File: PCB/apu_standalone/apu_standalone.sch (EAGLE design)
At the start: 95 parts, among them IC1 74AHC573, IC10 DAC, IC11 IS62C1024AL, IC12 ATMEGA2560, IC15 FT232RL, IC2 4050D, IC3 DS1307, IC4 LP298XS, IC5 S-SMP, IC6 S-DSP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

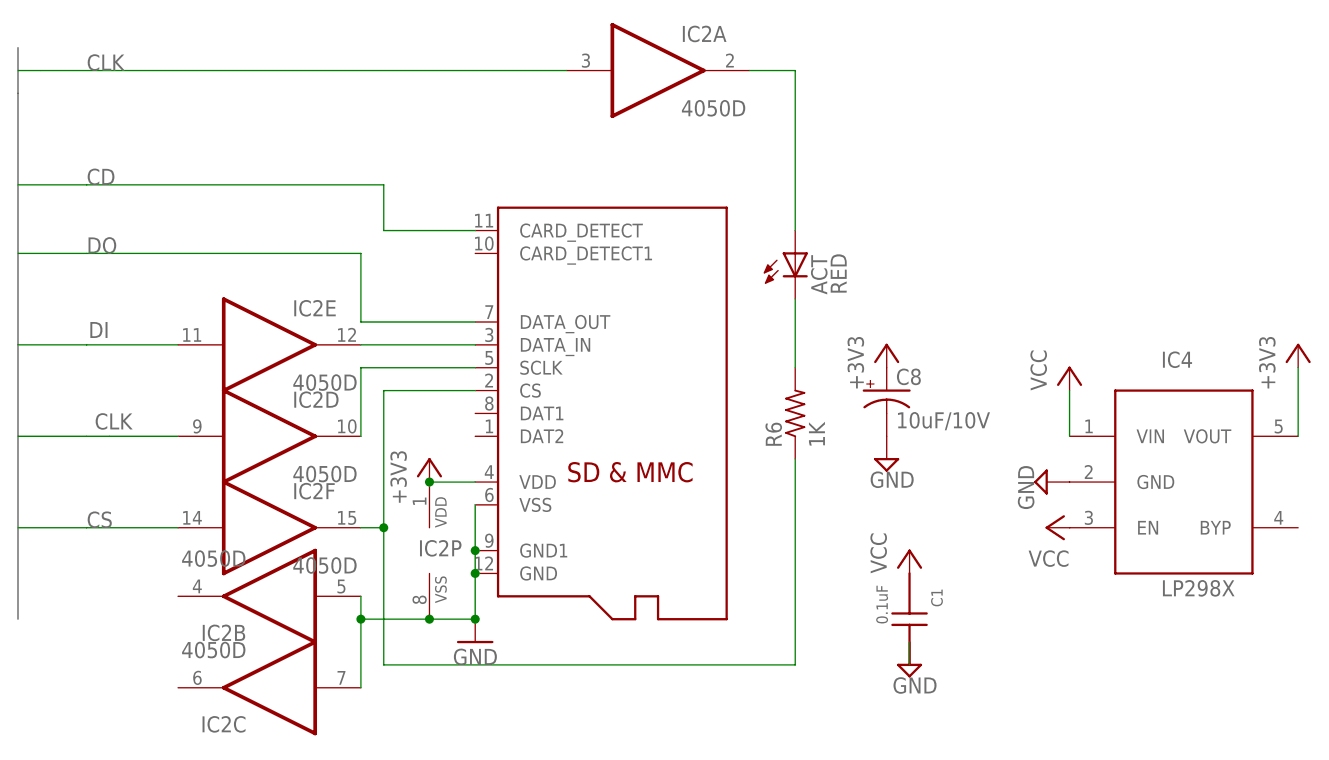
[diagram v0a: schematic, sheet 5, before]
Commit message: PC Side communications
Added various commands for a planned total rewrite of the PC side
client,.
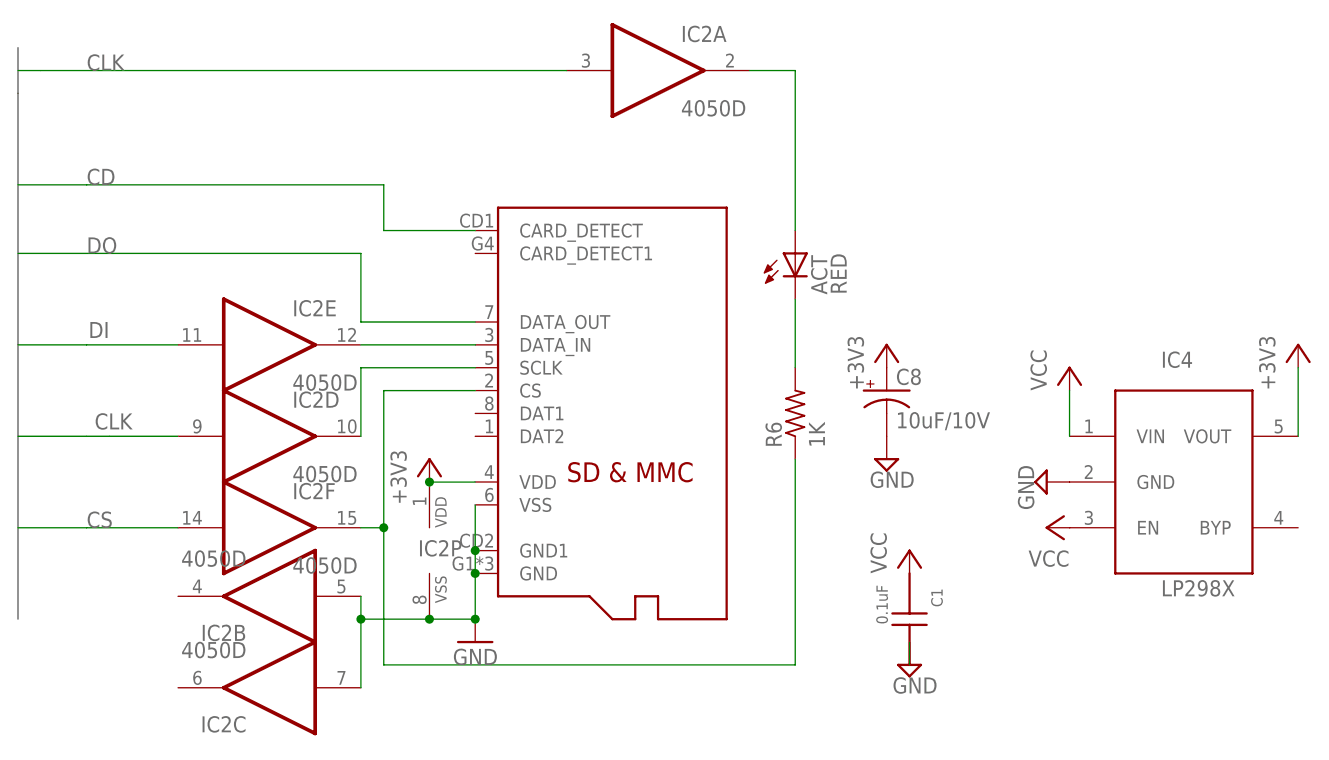
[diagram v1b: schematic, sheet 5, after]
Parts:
- X1: value MICROSDMOLEX -> MICROSDMOLEX-2; device adafruit:MICROSDMOLEX -> adafruit:MICROSDMOLEX-2
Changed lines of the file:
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@@
 <grid distance="0.1" unitdist="inch" unit="inch" style="lines" multiple="1" display="no" altdistance="0.01" altunitdist="inch" altunit="inch"/>
 <layers>
-<layer number="1" name="Top" color="4" fill="1" visible="no" active="no"/>
-<layer number="2" name="Route2" color="1" fill="3" visible="no" active="no"/>
-<layer number="3" name="Route3" color="4" fill="3" visible="no" active="no"/>
-<layer number="4" name="Route4" color="1" fill="4" visible="no" active="no"/>
-<layer number="5" name="Route5" color="4" fill="4" visible="no" active="no"/>
-<layer number="6" name="Route6" color="1" fill="8" visible="no" active="no"/>
-<layer number="7" name="Route7" color="4" fill="8" visible="no" active="no"/>
-<layer number="8" name="Route8" color="1" fill="2" visible="no" active="no"/>
-<layer number="9" name="Route9" color="4" fill="2" visible="no" active="no"/>
-<layer number="10" name="Route10" color="1" fill="7" visible="no" active="no"/>
-<layer number="11" name="Route11" color="4" fill="7" visible="no" active="no"/>
-<layer number="12" name="Route12" color="1" fill="5" visible="no" active="no"/>
-<layer number="13" name="Route13" color="4" fill="5" visible="no" active="no"/>
-<layer number="14" name="Route14" color="1" fill="6" visible="no" active="no"/>
-<layer number="15" name="Route15" color="4" fill="6" visible="no" active="no"/>
-<layer number="16" name="Bottom" color="1" fill="1" visible="no" active="no"/>
-<layer number="17" name="Pads" color="2" fill="1" visible="no" active="no"/>
-<layer number="18" name="Vias" color="2" fill="1" visible="no" active="no"/>
-<layer number="19" name="Unrouted" color="6" fill="1" visible="no" active="no"/>
-<layer number="20" name="Dimension" color="15" fill="1" visible="no" active="no"/>
-<layer number="21" name="tPlace" color="7" fill="1" visible="no" active="no"/>
-<layer number="22" name="bPlace" color="7" fill="1" visible="no" active="no"/>
-<layer number="23" name="tOrigins" color="15" fill="1" visible="no" active="no"/>
-<layer number="24" name="bOrigins" color="15" fill="1" visible="no" active="no"/>
-<layer number="25" name="tNames" color="7" fill="1" visible="no" active="no"/>
-<layer number="26" name="bNames" color="7" fill="1" visible="no" active="no"/>
-<layer number="27" name="tValues" color="7" fill="1" visible="no" active="no"/>
-<layer number="28" name="bValues" color="7" fill="1" visible="no" active="no"/>
+<layer number="1" name="Top" color="4" fill="1" visible="yes" active="no"/>
+<layer number="2" name="Route2" color="1" fill="3" visible="yes" active="no"/>
+<layer number="3" name="Route3" color="4" fill="3" visible="yes" active="no"/>
+<layer number="4" name="Route4" color="1" fill="4" visible="yes" active="no"/>
+<layer number="5" name="Route5" color="4" fill="4" visible="yes" active="no"/>
+<layer number="6" name="Route6" color="1" fill="8" visible="yes" active="no"/>
+<layer number="7" name="Route7" color="4" fill="8" visible="yes" active="no"/>
+<layer number="8" name="Route8" color="1" fill="2" visible="yes" active="no"/>
+<layer number="9" name="Route9" color="4" fill="2" visible="yes" active="no"/>
+<layer number="10" name="Route10" color="1" fill="7" visible="yes" active="no"/>
+<layer number="11" name="Route11" color="4" fill="7" visible="yes" active="no"/>
+<layer number="12" name="Route12" color="1" fill="5" visible="yes" active="no"/>
+<layer number="13" name="Route13" color="4" fill="5" visible="yes" active="no"/>
+<layer number="14" name="Route14" color="1" fill="6" visible="yes" active="no"/>
+<layer number="15" name="Route15" color="4" fill="6" visible="yes" active="no"/>
+<layer number="16" name="Bottom" color="1" fill="1" visible="yes" active="no"/>
+<layer number="17" name="Pads" color="2" fill="1" visible="yes" active="no"/>
+<layer number="18" name="Vias" color="22" fill="1" visible="yes" active="no"/>
+<layer number="19" name="Unrouted" color="6" fill="1" visible="yes" active="no"/>
+<layer number="20" name="Dimension" color="15" fill="1" visible="yes" active="no"/>
+<layer number="21" name="tPlace" color="7" fill="1" visible="yes" active="no"/>
+<layer number="22" name="bPlace" color="7" fill="1" visible="yes" active="no"/>
+<layer number="23" name="tOrigins" color="15" fill="1" visible="yes" active="no"/>
+<layer number="24" name="bOrigins" color="15" fill="1" visible="yes" active="no"/>
+<layer number="25" name="tNames" color="7" fill="1" visible="yes" active="no"/>
+<layer number="26" name="bNames" color="7" fill="1" visible="yes" active="no"/>
+<layer number="27" name="tValues" color="7" fill="1" visible="yes" active="no"/>
+<layer number="28" name="bValues" color="7" fill="1" visible="yes" active="no"/>
 <layer number="29" name="tStop" color="7" fill="3" visible="no" active="no"/>
 <layer number="30" name="bStop" color="7" fill="6" visible="no" active="no"/>
@@
 <layer number="35" name="tGlue" color="7" fill="4" visible="no" active="no"/>
 <layer number="36" name="bGlue" color="7" fill="5" visible="no" active="no"/>
-<layer number="37" name="tTest" color="7" fill="1" visible="no" active="no"/>
-<layer number="38" name="bTest" color="7" fill="1" visible="no" active="no"/>
+<layer number="37" name="tTest" color="7" fill="1" visible="yes" active="no"/>
+<layer number="38" name="bTest" color="7" fill="1" visible="yes" active="no"/>
 <layer number="39" name="tKeepout" color="4" fill="11" visible="no" active="no"/>
 <layer number="40" name="bKeepout" color="1" fill="11" visible="no" active="no"/>
@@
 <layer number="44" name="Drills" color="7" fill="1" visible="no" active="no"/>
 <layer number="45" name="Holes" color="7" fill="1" visible="no" active="no"/>
-<layer number="46" name="Milling" color="3" fill="1" visible="no" active="no"/>
-<layer number="47" name="Measures" color="7" fill="1" visible="no" active="no"/>
-<layer number="48" name="Document" color="7" fill="1" visible="no" active="no"/>
-<layer number="49" name="Reference" color="7" fill="1" visible="no" active="no"/>
-<layer number="50" name="dxf" color="7" fill="1" visible="no" active="no"/>
-<layer number="51" name="tDocu" color="7" fill="1" visible="no" active="no"/>
-<layer number="52" name="bDocu" color="7" fill="1" visible="no" active="no"/>
-<layer number="53" name="tGND_GNDA" color="7" fill="9" visible="no" active="no"/>
-<layer number="54" name="bGND_GNDA" color="1" fill="9" visible="no" active="no"/>
-<layer number="56" name="wert" color="7" fill="1" visible="no" active="no"/>
+<layer number="46" name="Milling" color="3" fill="1" visible="yes" active="no"/>
+<layer number="47" name="Measures" color="7" fill="1" visible="yes" active="no"/>
+<layer number="48" name="Document" color="7" fill="1" visible="yes" active="no"/>
+<layer number="49" name="Reference" color="7" fill="1" visible="yes" active="no"/>
+<layer number="50" name="dxf" color="7" fill="1" visible="yes" active="no"/>
+<layer number="51" name="tDocu" color="7" fill="1" visible="yes" active="no"/>
+<layer number="52" name="bDocu" color="7" fill="1" visible="yes" active="no"/>
+<layer number="53" name="tGND_GNDA" color="7" fill="9" visible="yes" active="no"/>
+<layer number="54" name="bGND_GNDA" color="1" fill="9" visible="yes" active="no"/>
+<layer number="56" name="wert" color="7" fill="1" visible="yes" active="no"/>
 <layer number="91" name="Nets" color="2" fill="1" visible="yes" active="yes"/>
 <layer number="92" name="Busses" color="1" fill="1" visible="yes" active="yes"/>
@@
 <part name="P+1" library="supply1" deviceset="VCC" device=""/>
 <part name="SUPPLY2" library="supply2" deviceset="GND" device=""/>
-<part name="X1" library="adafruit" deviceset="MICROSD" device="MOLEX"/>
+<part name="X1" library="adafruit" deviceset="MICROSD" device="MOLEX-2" value="MICROSDMOLEX-2"/>
 <part name="R2" library="adafruit" deviceset="R-US_" device="R0805" value="10K"/>
 <part name="R3" library="adafruit" deviceset="R-US_" device="R0805" value="10K"/>

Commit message: Changed micro-SD holder to push-in-push-out type.
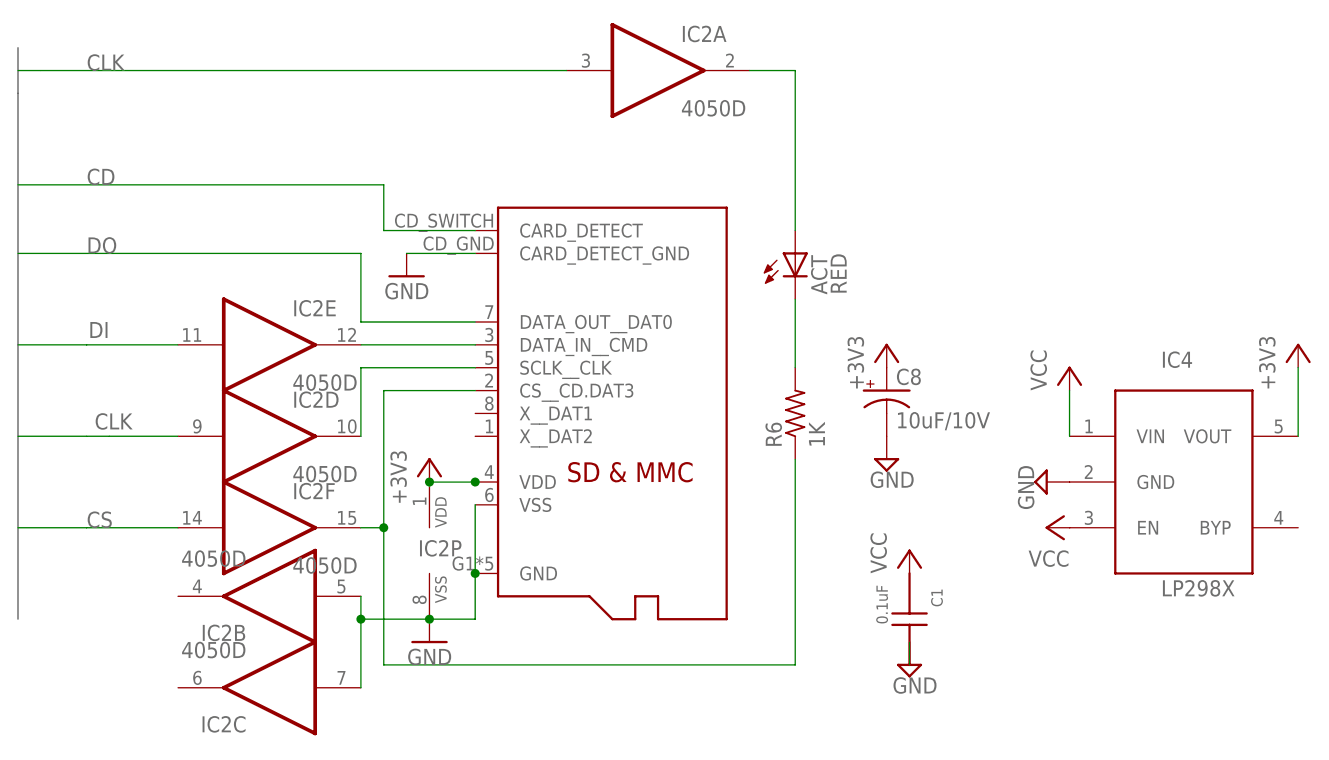
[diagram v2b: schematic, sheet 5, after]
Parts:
- removed X1: MICROSDMOLEX-2, adafruit:MICROSDMOLEX-2
- added U$1: MICROSD-2, adafruit:MICROSD-2
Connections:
- net +3V3: now also U$1.VDD; no longer X1.VDD
- net BUF_CLK: now also U$1.SCLK__CLK; no longer X1.SCLK
- net BUF_CS: now also U$1.CS__CD.DAT3; no longer X1.CS
- net BUF_DI: now also U$1.DATA_IN__CMD; no longer X1.DATA_IN
- net CD: now also U$1.CARD_DETECT; no longer X1.CARD_DETECT
- net DO: now also U$1.DATA_OUT__DAT0; no longer X1.DATA_OUT
- net GND: now also U$1.CARD_DETECT_GND, U$1.GND, U$1.VSS; no longer X1.GND, X1.GND1, X1.VSS

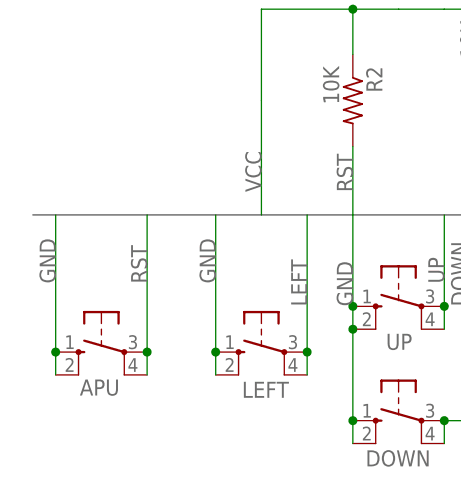
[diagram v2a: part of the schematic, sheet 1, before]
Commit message: APU reset button now has a 470 ohm series resistor to ground.
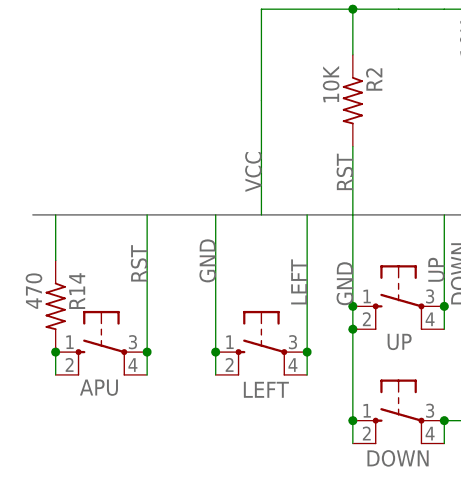
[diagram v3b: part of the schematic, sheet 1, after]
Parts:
- added R14: 470, adafruit:R-US_R0805
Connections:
- new net N$5: APU.S, APU.S1, R14.2
- net GND: now also R14.1; no longer APU.S, APU.S1
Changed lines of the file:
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@@
 <part name="GND14" library="supply1" deviceset="GND" device=""/>
 <part name="+3V1" library="supply1" deviceset="+3V3" device=""/>
+<part name="R14" library="adafruit" deviceset="R-US_" device="R0805" value="470"/>
 </parts>
 <sheets>
@@
 <instance part="R12" gate="G$1" x="63.5" y="43.18" rot="R270"/>
 <instance part="R13" gate="G$1" x="58.42" y="48.26" rot="R270"/>
+<instance part="R14" gate="G$1" x="10.16" y="20.32" rot="R270"/>
 </instances>
 <busses>
@@
 <wire x1="175.26" y1="22.86" x2="165.1" y2="22.86" width="0.1524" layer="91"/>
 <label x="167.64" y="22.86" size="1.778" layer="95"/>
-</segment>
-<segment>
-<pinref part="APU" gate="1" pin="S"/>
-<wire x1="10.16" y1="15.24" x2="10.16" y2="30.48" width="0.1524" layer="91"/>
-<pinref part="APU" gate="1" pin="S1"/>
-<wire x1="10.16" y1="15.24" x2="10.16" y2="12.7" width="0.1524" layer="91"/>
-<junction x="10.16" y="15.24"/>
-<label x="10.16" y="22.86" size="1.778" layer="95" rot="R90"/>
 </segment>
 <segment>
@@
 <wire x1="124.46" y1="50.8" x2="99.06" y2="50.8" width="0.1524" layer="91"/>
 <label x="101.6" y="50.8" size="1.778" layer="95"/>
+</segment>
+<segment>
+<pinref part="R14" gate="G$1" pin="1"/>
+<wire x1="10.16" y1="25.4" x2="10.16" y2="30.48" width="0.1524" layer="91"/>
 </segment>
 </net>
@@
 </segment>
 </net>
+<net name="N$5" class="0">
+<segment>
+<pinref part="APU" gate="1" pin="S"/>
+<pinref part="R14" gate="G$1" pin="2"/>
+<pinref part="APU" gate="1" pin="S1"/>
+<wire x1="10.16" y1="15.24" x2="10.16" y2="12.7" width="0.1524" layer="91"/>
+<junction x="10.16" y="15.24"/>
+</segment>
+</net>
